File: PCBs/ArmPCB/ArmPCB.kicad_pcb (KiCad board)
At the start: 2 copper layers, 58 x 47.5 mm, 28 parts, among them J1 Conn_02x07_Odd_Even, J10 Conn_01x04_Pin, J2 Conn_02x08_Odd_Even, J3 Conn_02x08_Odd_Even, J4 Conn_01x04_Pin, J5 Conn_01x02_Pin, J6 Conn_01x03_Pin, J7 Conn_01x03_Pin, J8 Conn_01x03_Pin, J9 Conn_01x04_Pin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

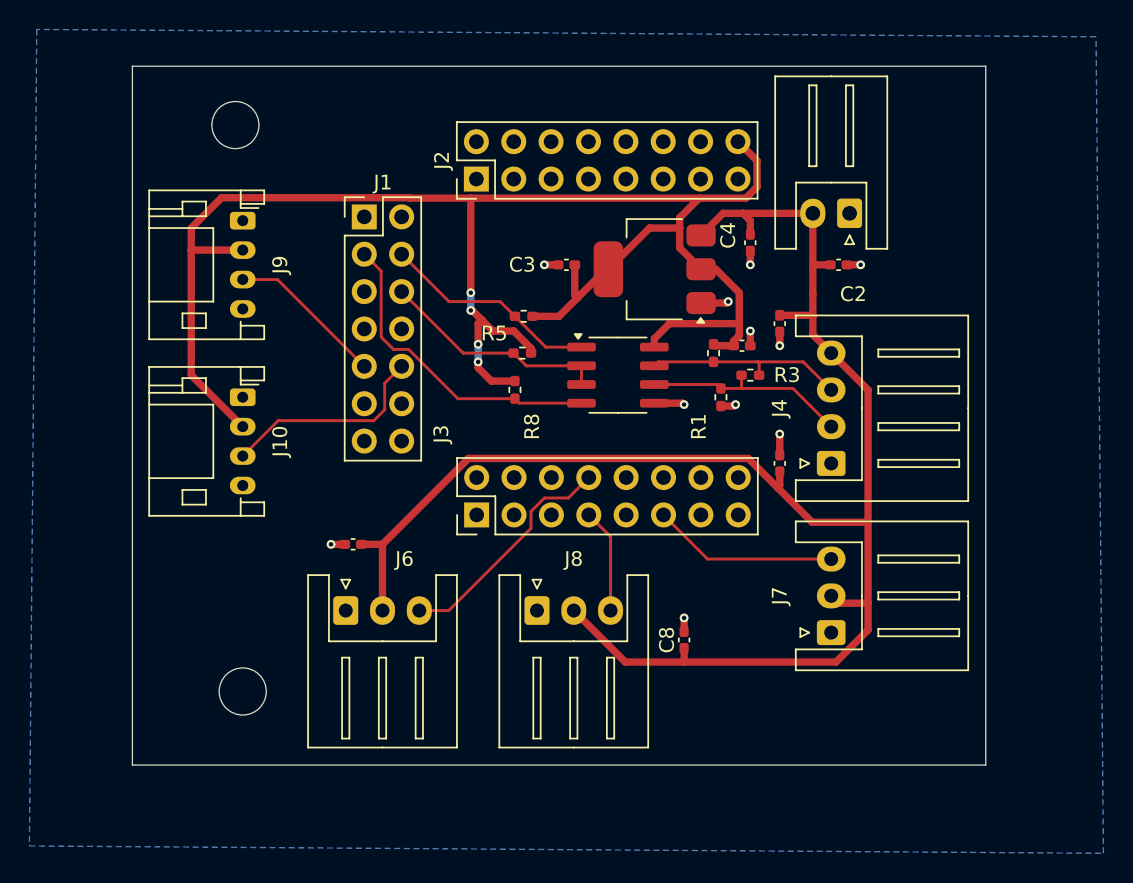
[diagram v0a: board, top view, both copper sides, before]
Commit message: Base_Arm_PCB JST FIX
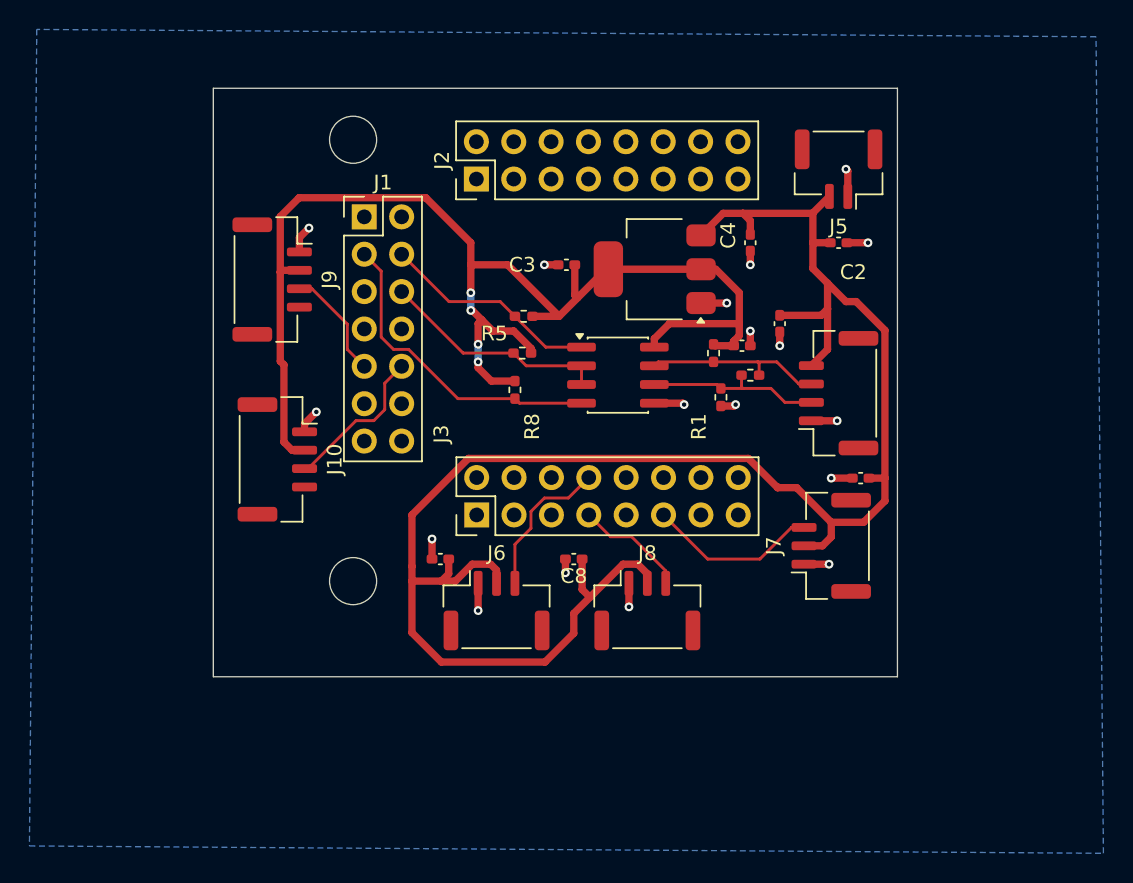
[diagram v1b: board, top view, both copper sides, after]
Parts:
- J10, J9: footprint Connector_JST:JST_PH_S4B-PH-K_1x04_P2.00mm_Horizontal -> Connector_JST:JST_GH_SM04B-GHS-TB_1x04-1MP_P1.25mm_Horizontal
- J4: footprint Connector_JST:JST_XH_S4B-XH-A_1x04_P2.50mm_Horizontal -> Connector_JST:JST_GH_SM04B-GHS-TB_1x04-1MP_P1.25mm_Horizontal
- J5: footprint Connector_JST:JST_XH_S2B-XH-A_1x02_P2.50mm_Horizontal -> Connector_JST:JST_GH_SM02B-GHS-TB_1x02-1MP_P1.25mm_Horizontal
- J6, J7, J8: footprint Connector_JST:JST_XH_S3B-XH-A_1x03_P2.50mm_Horizontal -> Connector_JST:JST_GH_SM03B-GHS-TB_1x03-1MP_P1.25mm_Horizontal
- moved H1 10.6 mm to (125.5, 84.0)
- moved J6 10.2 mm to (135.2, 86.0)
- moved C8 9.30 mm to (140.5, 82.5), turned to 180 degrees
- moved H2 8.06 mm to (125.5, 54.0)
- moved J8 7.50 mm to (145.5, 86.0)
- moved C6 6.02 mm to (131.4, 82.5)
- moved J7 5.90 mm to (158.0, 81.6)
- moved C7 5.59 mm to (160.0, 77.0), turned to 0 degrees
- moved J10 4.83 mm to (120.3, 75.7)
- moved J4 4.80 mm to (158.5, 71.2)
- moved J9 4.47 mm to (120.0, 63.5)
- moved J5 3.09 mm to (158.5, 56.0)
- moved C2 1.50 mm to (158.5, 61.0)
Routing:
- net +3.3V: track 117.0 -> 87.2 mm
- net 5V: track 112.4 -> 125.6 mm
- net GND: track 13.0 -> 26.2 mm, vias 11 -> 18
- net /27: track 15.9 -> 10.2 mm
- net /20: track 14.4 -> 10.5 mm
- net /21: track 10.7 -> 7.60 mm
- net /A+: track 14.2 -> 12.1 mm
- net /B-: track 13.9 -> 12.4 mm
- net /30: track 12.6 -> 11.7 mm
- net /26: track 7.11 -> 7.65 mm
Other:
- board size 58 x 47.5 mm -> 46.5 x 40 mm
